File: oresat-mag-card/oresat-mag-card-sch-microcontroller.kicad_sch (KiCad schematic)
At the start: 31 parts, among them U7 MCXN947VKLT, U8 TCAN330, Y1 24 MHz

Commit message: Small update
removed all traces containing widths of .127 and widened to .2, and some other small misc items
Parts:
- R45, R46, R48: footprint Resistor_SMD:R_0603_1608Metric -> oresat-passives:c_0603-SMALL
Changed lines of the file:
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@@
 			)
 		)
-		(property "Footprint" "Resistor_SMD:R_0603_1608Metric"
+		(property "Footprint" "oresat-passives:c_0603-SMALL"
 			(at 182.88 284.48 0)
 			(effects
@@
 			)
 		)
-		(property "Footprint" "Resistor_SMD:R_0603_1608Metric"
+		(property "Footprint" "oresat-passives:c_0603-SMALL"
 			(at 361.95 280.67 0)
 			(effects
@@
 			)
 		)
-		(property "Footprint" "Resistor_SMD:R_0603_1608Metric"
+		(property "Footprint" "oresat-passives:c_0603-SMALL"
 			(at 370.84 280.67 0)
 			(effects

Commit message: Update
Updated footprints, symbols, and pcb layout to have IMU in center of board.
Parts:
- C20: footprint oresat-passives:c_0603-SMALL -> oresat-passives:0805-B-NOSILK
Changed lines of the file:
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@@
 			)
 		)
-		(property "Footprint" "oresat-passives:c_0603-SMALL"
+		(property "Footprint" "oresat-passives:0805-B-NOSILK"
 			(at 438.15 198.12 0)
 			(effects

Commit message: Final touch ups
Added new j3 connector, and final touch ups
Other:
- moved on the sheet: C15
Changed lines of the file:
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@@
 	(text "CAN Transceiver"
 		(exclude_from_sim no)
-		(at 218.948 250.19 0)
+		(at 218.948 243.84 0)
 		(effects
 			(font
@@
 	)
 	(junction
-		(at 207.01 262.89)
+		(at 207.01 251.46)
 		(diameter 0)
 		(color 0 0 0 0)
@@
 	(wire
 		(pts
-			(xy 207.01 262.89) (xy 207.01 264.16)
-		)
-		(stroke
-			(width 0)
-			(type default)
-		)
-	)
-	(wire
-		(pts
 			(xy 334.01 257.81) (xy 353.06 257.81)
 		)
@@
 	(wire
 		(pts
+			(xy 222.25 257.81) (xy 222.25 259.08)
+		)
+		(stroke
+			(width 0)
+			(type default)
+		)
+	)
+	(wire
+		(pts
 			(xy 425.45 214.63) (xy 425.45 215.9)
 		)
@@
 	(wire
 		(pts
-			(xy 222.25 262.89) (xy 224.79 262.89)
+			(xy 222.25 251.46) (xy 222.25 252.73)
 		)
 		(stroke
@@
 	(wire
 		(pts
-			(xy 207.01 262.89) (xy 217.17 262.89)
+			(xy 207.01 251.46) (xy 222.25 251.46)
 		)
 		(stroke
@@
 	(wire
 		(pts
-			(xy 207.01 261.62) (xy 207.01 262.89)
+			(xy 207.01 250.19) (xy 207.01 251.46)
 		)
 		(stroke
@@
 	(wire
 		(pts
+			(xy 207.01 251.46) (xy 207.01 264.16)
+		)
+		(stroke
+			(width 0)
+			(type default)
+		)
+	)
+	(wire
+		(pts
 			(xy 356.87 128.27) (xy 369.57 128.27)
 		)
@@
 	(symbol
 		(lib_id "oresat-power:3.3V")
-		(at 207.01 261.62 0)
+		(at 207.01 250.19 0)
 		(unit 1)
 		(exclude_from_sim no)
@@
 		(fields_autoplaced yes)
 		(property "Reference" "#3V04"
-			(at 207.01 265.43 0)
+			(at 207.01 254 0)
 			(effects
 				(font
@@
 		)
 		(property "Value" "3.3V"
-			(at 207.01 256.54 0)
+			(at 207.01 245.11 0)
 			(effects
 				(font
@@
 		)
 		(property "Footprint" ""
-			(at 207.01 261.62 0)
+			(at 207.01 250.19 0)
 			(effects
 				(font
@@
 		)
 		(property "Datasheet" ""
-			(at 207.01 261.62 0)
+			(at 207.01 250.19 0)
 			(effects
 				(font
@@
 		)
 		(property "Description" "Power symbol creates a global label with name \"3.3V\""
-			(at 207.01 261.62 0)
+			(at 207.01 250.19 0)
 			(effects
 				(font
@@
 		)
 		(pin "2"
+			(alternate "ISP-UART_TXD")
 		)
 		(pin "10"
+			(alternate "XTAL48M ")
 		)
 		(pin "99"
@@
 		)
 		(pin "1"
+			(alternate "ISP-UART_RXD")
 		)
 		(pin "3"
@@
 		)
 		(pin "6"
+			(alternate "FLEXIO0_D21 ")
 		)
 		(pin "8"
@@
 		)
 		(pin "11"
+			(alternate "EXTAL48M ")
 		)
 		(pin "15"
@@
 	(symbol
 		(lib_id "Device:C_Small")
-		(at 219.71 262.89 90)
+		(at 222.25 255.27 0)
 		(unit 1)
 		(exclude_from_sim no)
@@
 		(dnp no)
 		(property "Reference" "C15"
-			(at 218.5041 260.5659 0)
+			(at 224.5741 254.0641 0)
 			(effects
 				(font
@@
 		)
 		(property "Value" "100n"
-			(at 220.9284 260.5659 0)
+			(at 224.5741 256.4884 0)
 			(effects
 				(font
@@
 		)
 		(property "Footprint" "oresat-passives:c_0603-SMALL"
-			(at 219.71 262.89 0)
+			(at 222.25 255.27 0)
 			(effects
 				(font
@@
 		)
 		(property "Datasheet" "https://mm.digikey.com/Volume0/opasdata/d220001/medias/docus/1068/TMK107BJ104KAHT_SS.pdf"
-			(at 219.71 262.89 0)
+			(at 222.25 255.27 0)
 			(effects
 				(font
@@
 		)
 		(property "Description" "100 nF (0.1µF) ±10% 25V Ceramic Capacitor X5R 0603 (1608 Metric)"
-			(at 219.71 262.89 0)
+			(at 222.25 255.27 0)
 			(effects
 				(font
@@
 		)
 		(property "MFR" "Taiyo Yuden"
-			(at 219.71 262.89 0)
+			(at 222.25 255.27 0)
 			(effects
 				(font
@@
 		)
 		(property "MPN" "TMK107BJ104KAHT"
-			(at 219.71 262.89 0)
+			(at 222.25 255.27 0)
 			(effects
 				(font
@@
 		)
 		(property "DIS" "DigiKey"
-			(at 219.71 262.89 0)
+			(at 222.25 255.27 0)
 			(effects
 				(font
@@
 		)
 		(property "DPN" "587-3472-1-ND"
-			(at 219.71 262.89 0)
+			(at 222.25 255.27 0)
 			(effects
 				(font
@@
 		)
 		(property "DIST" ""
-			(at 219.71 262.89 0)
+			(at 222.25 255.27 0)
 			(effects
 				(font
@@
 		)
 		(pin "35"
+			(alternate "FLEXIO0_D20")
 		)
 		(pin "50"
@@
 		)
 		(pin "26"
+			(alternate "ADC1_A0 ")
 		)
 		(pin "28"
 		)
 		(pin "38"
+			(alternate "FLEXIO0_D24")
 		)
 		(pin "43"
@@
 		)
 		(pin "40"
+			(alternate "FLEXIO0_D27")
 		)
 		(pin "48"
@@
 		)
 		(pin "39"
+			(alternate "FLEXIO0_D25")
 		)
 		(pin "49"
 		)
 		(pin "36"
+			(alternate "FLEXIO0_D21")
 		)
 		(pin "41"
+			(alternate "FLEXIO0_D28")
 		)
 		(pin "25"
@@
 		(lib_name "GND_1")
 		(lib_id "power:GND")
-		(at 224.79 262.89 0)
+		(at 222.25 259.08 0)
 		(unit 1)
 		(exclude_from_sim no)
@@
 		(dnp no)
 		(property "Reference" "#GND037"
-			(at 224.79 269.24 0)
+			(at 222.25 265.43 0)
 			(effects
 				(font
@@
 		)
 		(property "Value" "GND"
-			(at 224.79 266.7 0)
+			(at 222.25 262.89 0)
 			(effects
 				(font
@@
 		)
 		(property "Footprint" ""
-			(at 224.79 262.89 0)
+			(at 222.25 259.08 0)
 			(effects
 				(font
@@
 		)
 		(property "Datasheet" ""
-			(at 224.79 262.89 0)
+			(at 222.25 259.08 0)
 			(effects
 				(font
@@
 		)
 		(property "Description" "Power symbol creates a global label with name \"GND\" , ground"
-			(at 224.79 262.89 0)
+			(at 222.25 259.08 0)
 			(effects
 				(font

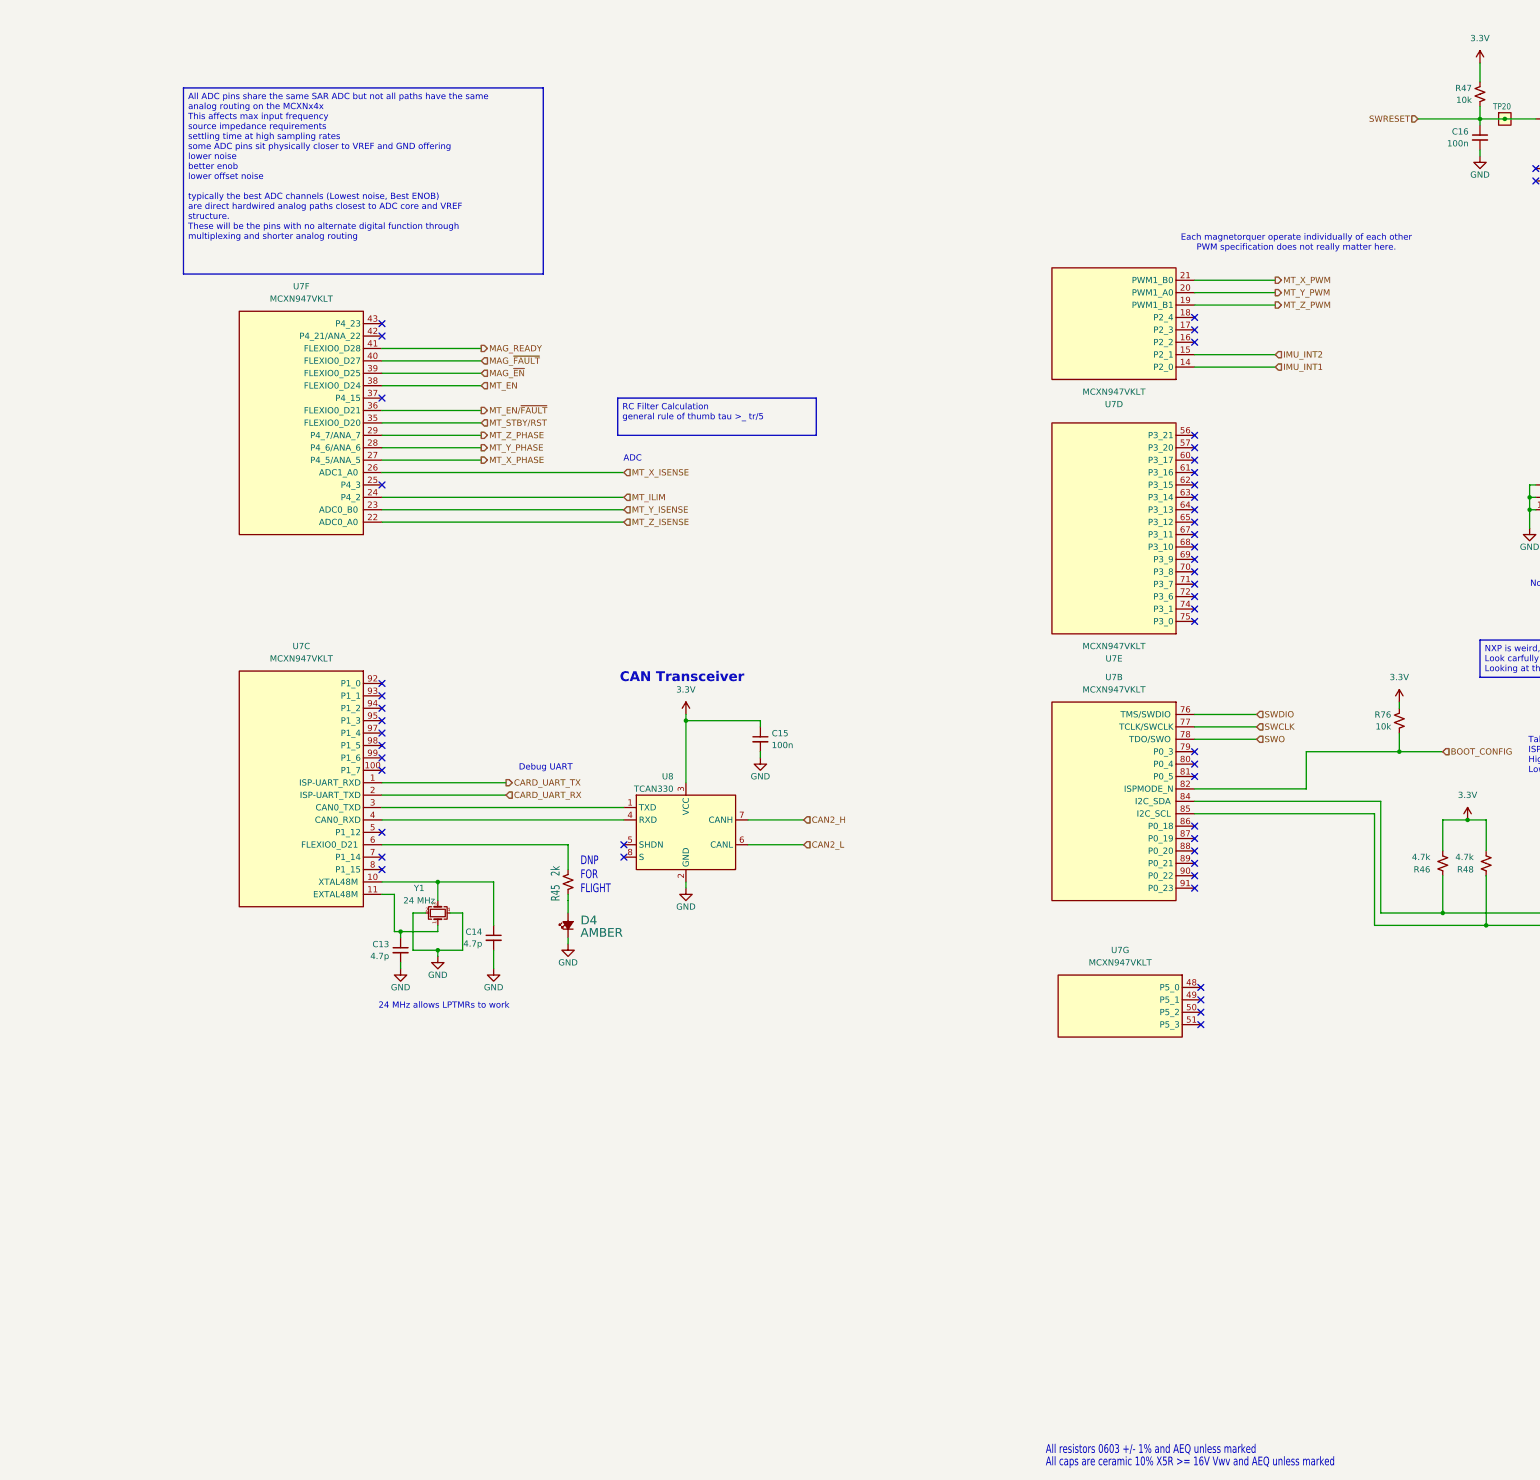
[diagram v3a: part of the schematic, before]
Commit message: Schematic polish, fixed UART TX/RX mixup, imported into layout
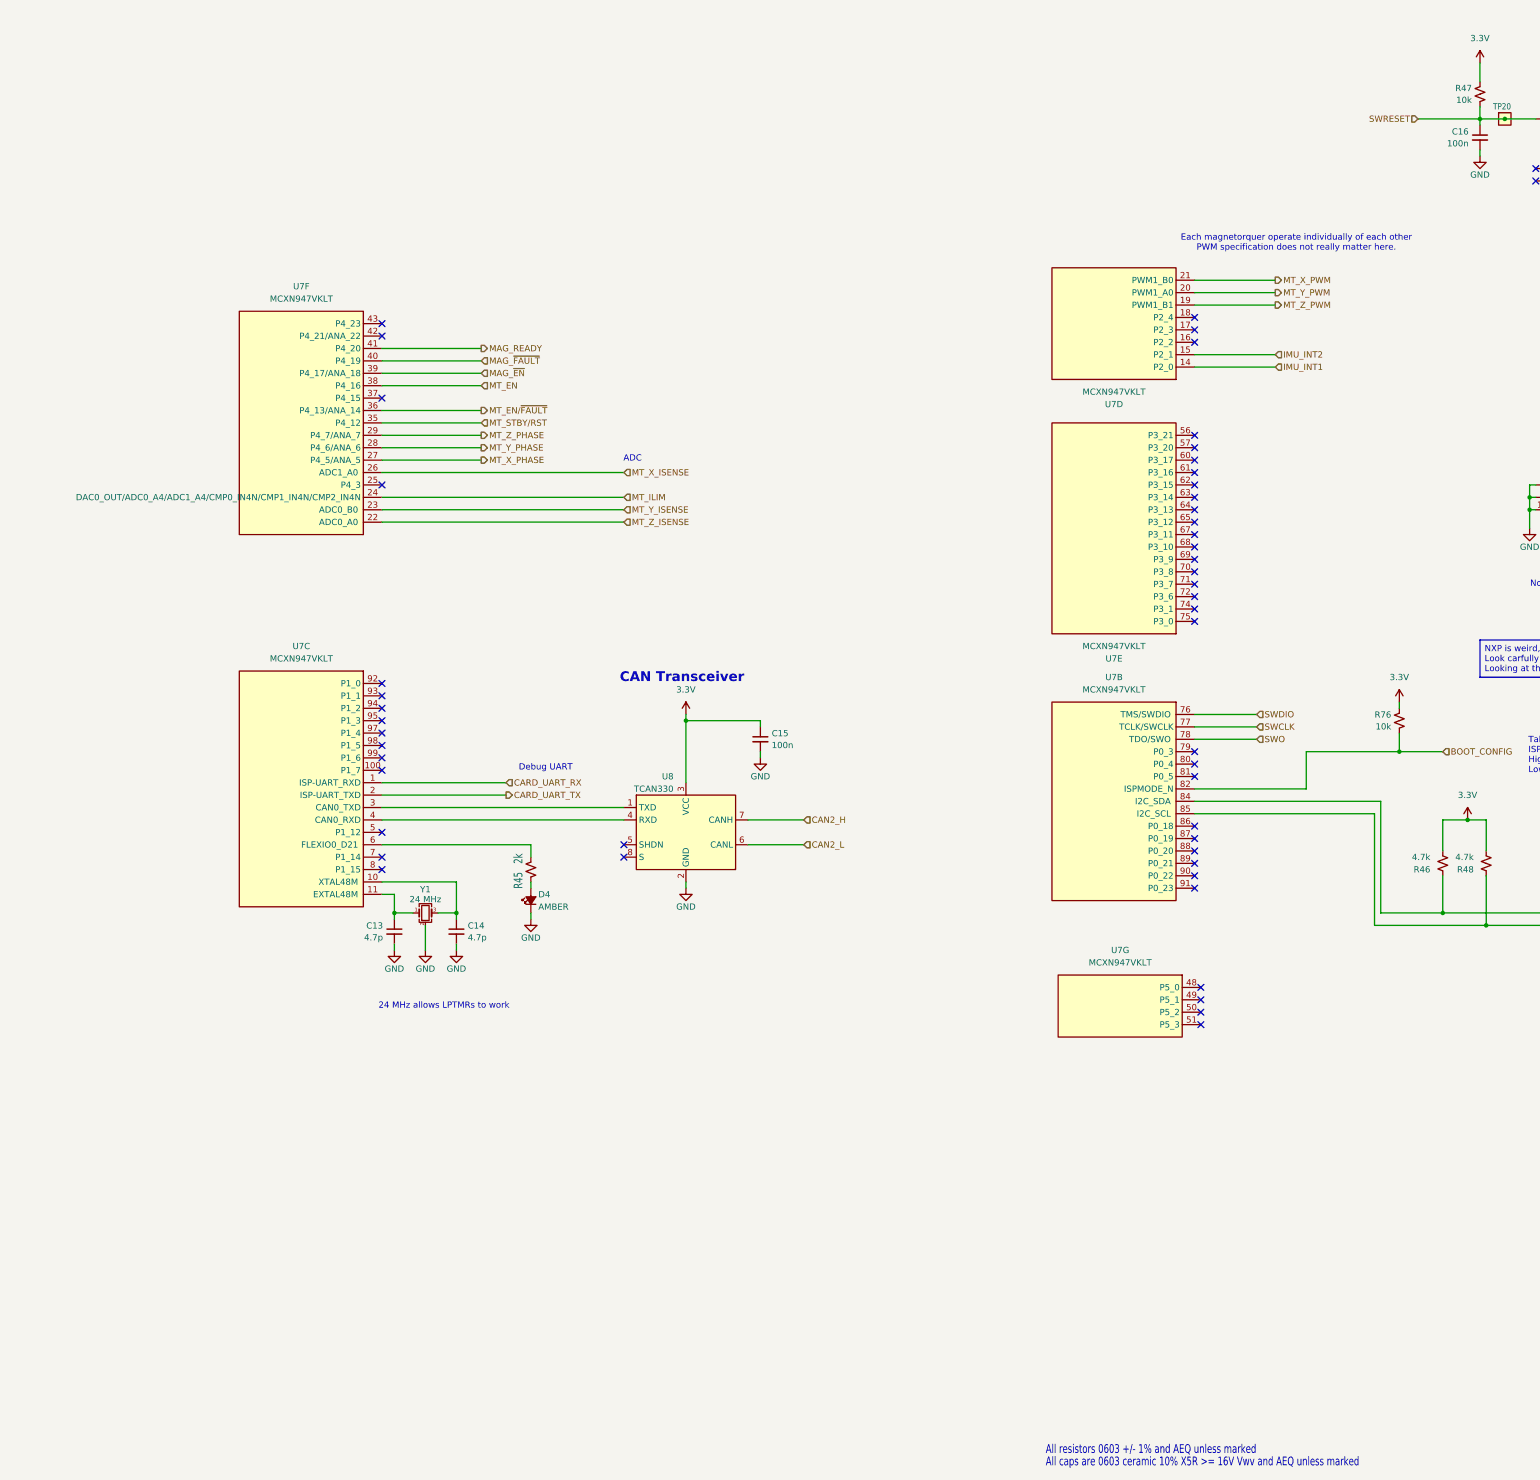
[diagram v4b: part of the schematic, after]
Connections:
- net CARD_UART_RX: now also U7.1 (P1_8); no longer U7.2 (P1_9)
- net CARD_UART_TX: now also U7.2 (P1_9); no longer U7.1 (P1_8)
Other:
- note added: "All caps are 0603 ceramic 10% X5R >= 16V Vwv and AEQ unless marked"
- note removed: "All caps are ceramic 10% X5R >= 16V Vwv and AEQ unless marked"
- note removed: "DNP FOR FLIGHT"
- company: Edward Tsoi -> Portland State Aerospace Society
- title: MCXN Microcontroller -> OreSat Mag Card
- moved on the sheet: C13, C14, D4, R45, U7F

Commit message: No DRC errors
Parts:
- C13, C14, C15, C16, C17, C18, C19, C21, C22, C23, C24, C25, C26, C27, C28, C29, C30, C70, R45, R46, R48: footprint oresat-passives:c_0603-SMALL -> oresat-passives:0603-C-NOSILK
- R76: footprint Resistor_SMD:R_0603_1608Metric -> oresat-passives:0603-C-NOSILK
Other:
- moved on the sheet: C13, C14, C15, C16, C17, C18, C19, C20, C21, C22, C23, C24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

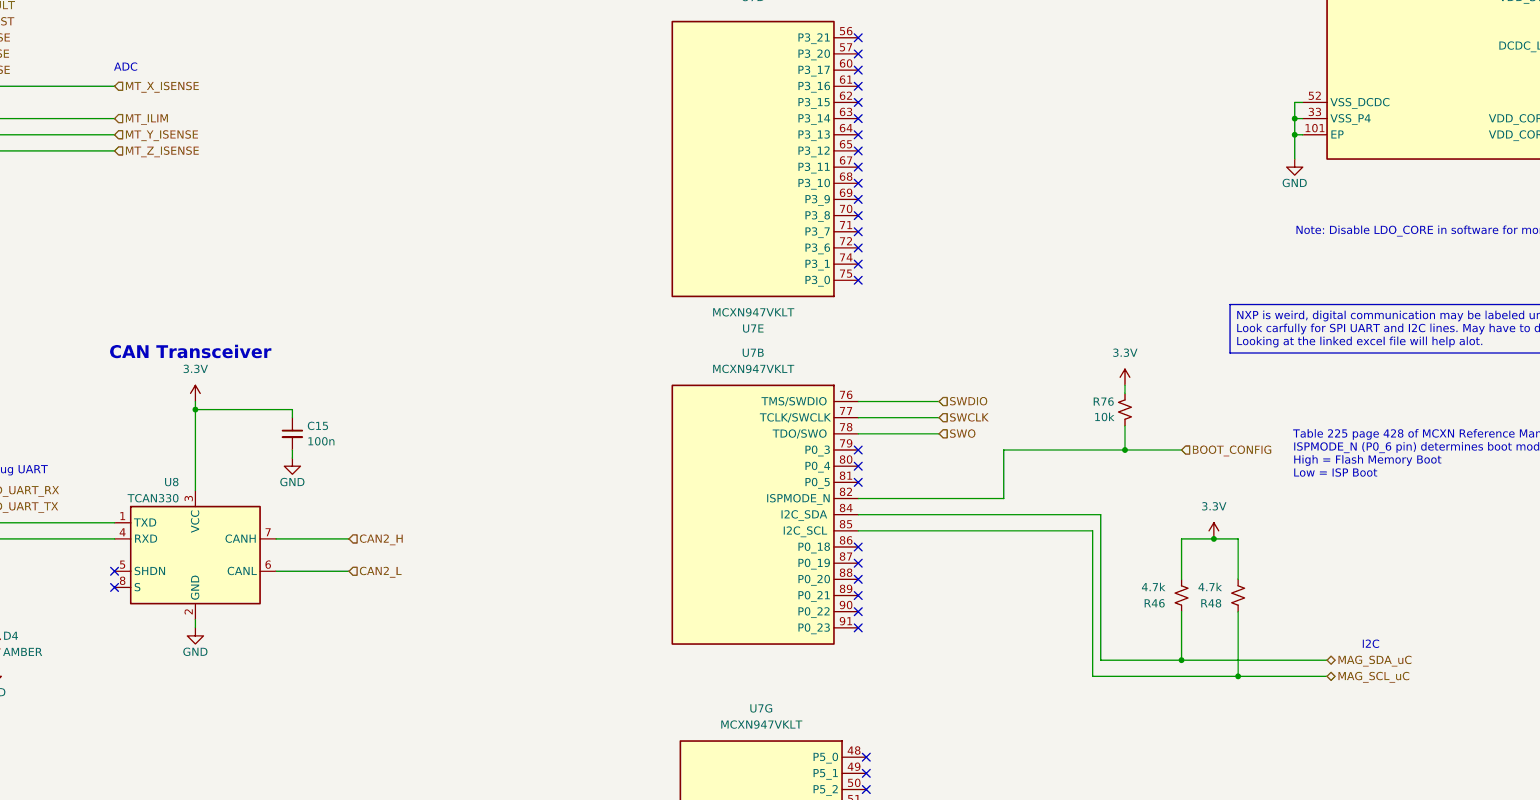
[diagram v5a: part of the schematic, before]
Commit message: Moved to independent MT connectors using pico EZ connectors, and re-laid out the STSPIN250s to be more best-practices.
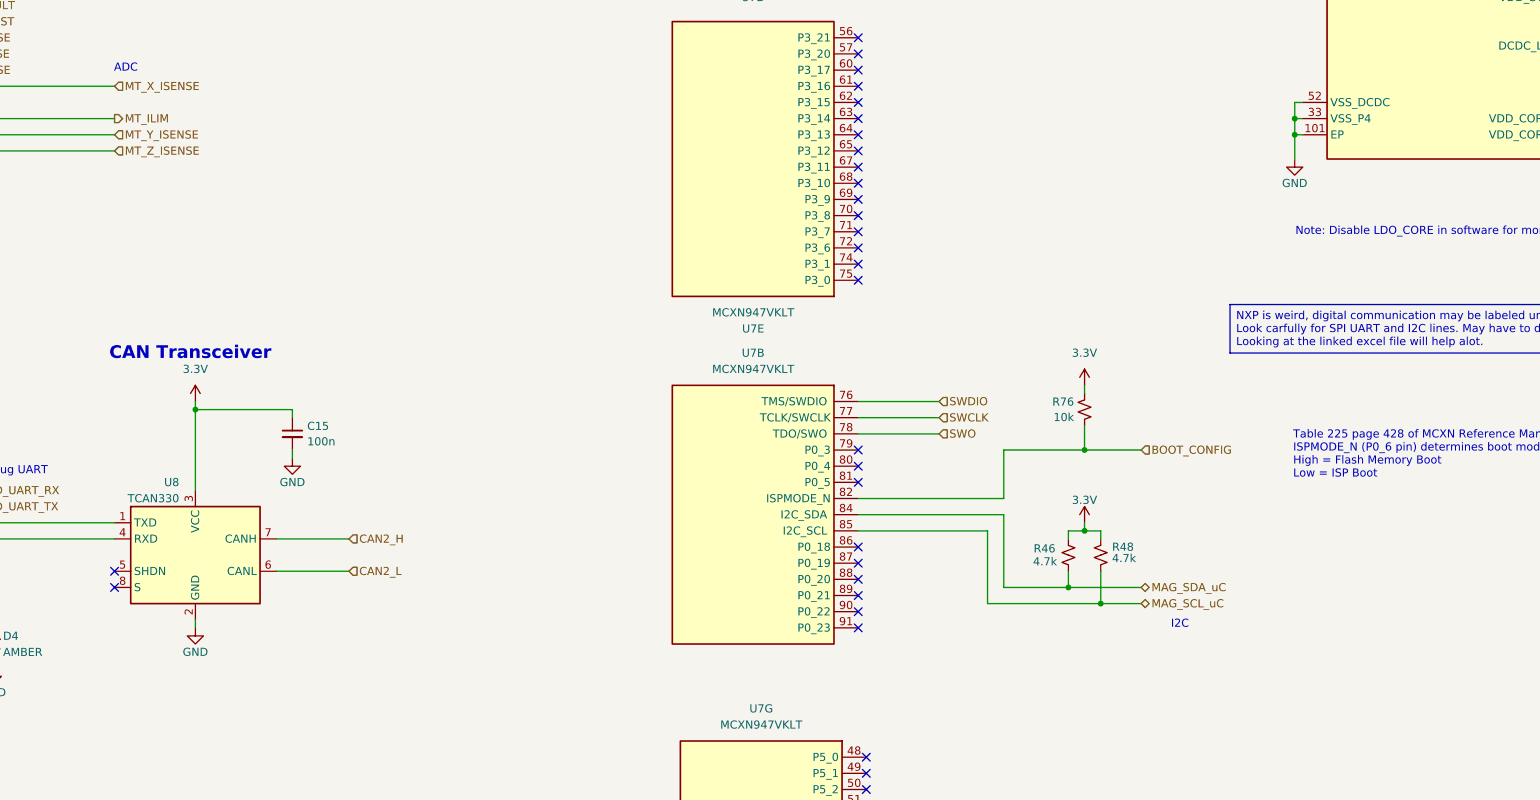
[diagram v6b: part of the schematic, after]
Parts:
- C13, C14: DIST (none) -> DigiKey; DPN 490-GRM1885C1H4R7WA01DCT-ND -> 399-15924-1-ND; MFR Murata -> KEMET; MPN GRM1885C1H4R7WA01D -> C0603C479D5GACAUTO
- C15, C16, C17, C23, C24, C25, C26, C27, C28, C29, C30, C70: DIST (none) -> DigiKey; DPN 587-3472-1-ND -> 399-6856-1-ND; MFR Taiyo Yuden -> KEMET; MPN TMK107BJ104KAHT -> C0603C104K5RACAUTO
- C18, C19: DIST (none) -> DigiKey; DPN 587-4332-1-ND -> 490-GRT188C71C475KE13DCT-ND; MFR Taiyo Yuden -> Murata Electronics; MPN EMK107BBJ475KAHT -> GRT188C71C475KE13D
- C20: DIST (none) -> DigiKey; DPN 445-12661-1-ND -> 445-16116-1-ND; MPN CGA4J1X5R1C685K125AC -> CGA4J3X7S1A685K125AB
- C21: DIST (none) -> DigiKey; DPN 587-4929-1-ND -> 490-GRT188C71E225KE13DCT-ND; MFR Taiyo Yuden -> Murata Electronics; MPN TMK107BBJ225MAHT -> GRT188C71E225KE13D
- C22: DIST (none) -> DigiKey; DPN 587-3473-1-ND -> 490-GRT188R71E105KE13DCT-ND; MFR Taiyo Yuden -> Murata Electronics; MPN TMK107BJ105KAHT -> GRT188R71E105KE13D
- D4, U8: DIST (none) -> DigiKey
- R46, R48: DIST (none) -> DigiKey; DPN (none) -> RMCF0603FT4K70CT-ND; MFR (none) -> Stackpole Electronics; MPN (none) -> RMCF0603FT4K70
- R47, R76: DIST (none) -> DigiKey; MFR Stackpole Electronics Inc -> Stackpole Electronics
- U7: DIST (none) -> DigiKey; DPN (none) -> 568-MCXN947VDFT-ND; MPN MCXN947VKLT -> MCXN947VDFT
- Y1: DIST (none) -> DigiKey; MFR Wurth -> Wurth Electronics
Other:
- moved on the sheet: R46, R48, R76
